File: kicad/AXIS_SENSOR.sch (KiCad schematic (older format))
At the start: 4 parts, among them U10 MPU6500

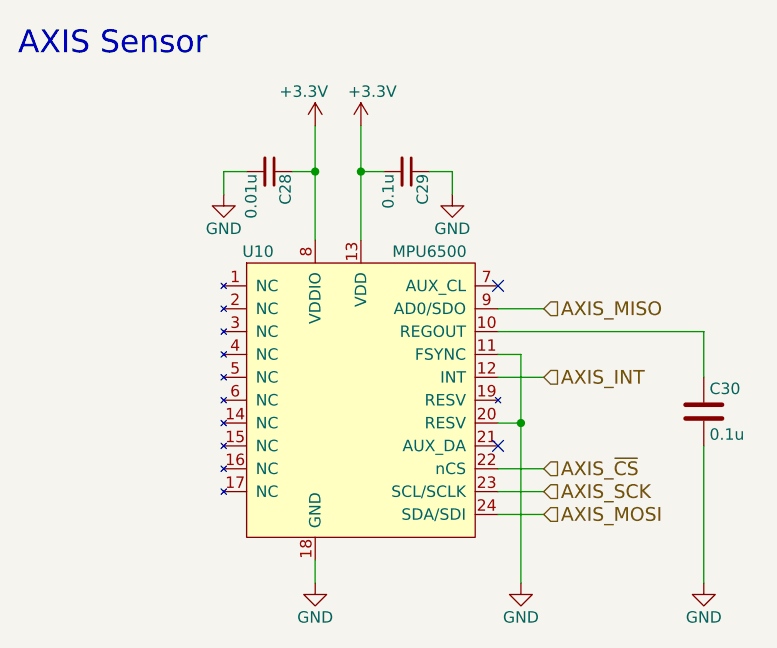
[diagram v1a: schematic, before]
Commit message: 回路図を修正
電源スイッチにPchFETを挿入
赤外線LED用FETのゲートをプルダウン
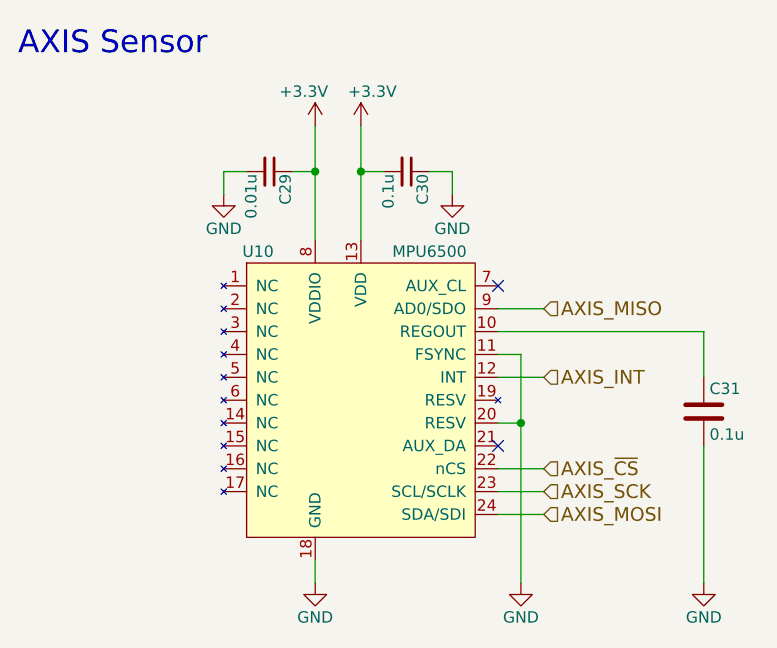
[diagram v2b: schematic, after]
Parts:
- renumbered C28 to C29, C29 to C30, C30 to C31
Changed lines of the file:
@@
 EESchema Schematic File Version 2
+LIBS:KERISEv1-rescue
 LIBS:74xgxx
 LIBS:74xx
@@
 LIBS:cmos4000
 LIBS:conn
-LIBS:connectors
 LIBS:contrib
 LIBS:cypress
@@
 LIBS:ftdi
 LIBS:gennum
-LIBS:graphic
 LIBS:hc11
-LIBS:ic-cpu
-LIBS:ic-io
-LIBS:ic-misc
-LIBS:ic-power
 LIBS:intel
 LIBS:interface
@@
 LIBS:Lattice
 LIBS:linear
-LIBS:logo
 LIBS:maxim
 LIBS:memory
@@
 LIBS:opto
 LIBS:Oscillators
-LIBS:passive
 LIBS:philips
 LIBS:power
@@
 LIBS:Zilog
 LIBS:KERISEv1
-LIBS:kerikun11
 LIBS:KERISEv1-cache
 EELAYER 25 0
@@
 $EndDescr
 $Comp
-L +3.3V #PWR78
+L +3.3V #PWR84
 U 1 1 57CCAAD0
 P 5700 2700
-F 0 "#PWR78" H 5700 2550 50  0001 C CNN
+F 0 "#PWR84" H 5700 2550 50  0001 C CNN
 F 1 "+3.3V" H 5750 2850 50  0000 C CNN
 F 2 "" H 5700 2700 50  0000 C CNN
@@
 	5700 2700 5700 3200
 $Comp
-L GND #PWR81
+L GND #PWR83
 U 1 1 57CCAAFB
 P 5500 4700
-F 0 "#PWR81" H 5500 4450 50  0001 C CNN
+F 0 "#PWR83" H 5500 4450 50  0001 C CNN
 F 1 "GND" H 5500 4550 50  0000 C CNN
 F 2 "" H 5500 4700 50  0000 C CNN
@@
 AXIS_MISO
 $Comp
-L GND #PWR82
+L GND #PWR86
 U 1 1 57CCAB79
 P 6400 4700
-F 0 "#PWR82" H 6400 4450 50  0001 C CNN
+F 0 "#PWR86" H 6400 4450 50  0001 C CNN
 F 1 "GND" H 6400 4550 50  0000 C CNN
 F 2 "" H 6400 4700 50  0000 C CNN
@@
 	6400 3700 6300 3700
 $Comp
-L C C30
+L C C31
 U 1 1 57CCABB6
 P 7200 3950
-F 0 "C30" H 7225 4050 50  0000 L CNN
+F 0 "C31" H 7225 4050 50  0000 L CNN
 F 1 "0.1u" H 7225 3850 50  0000 L CNN
 F 2 "Capacitors_SMD:C_0603" H 7238 3800 50  0001 C CNN
@@
 	7200 3600 6300 3600
 $Comp
-L GND #PWR83
+L GND #PWR87
 U 1 1 57CCAC2E
 P 7200 4700
-F 0 "#PWR83" H 7200 4450 50  0001 C CNN
+F 0 "#PWR87" H 7200 4450 50  0001 C CNN
 F 1 "GND" H 7200 4550 50  0000 C CNN
 F 2 "" H 7200 4700 50  0000 C CNN
@@
 	6500 4400 6300 4400
 $Comp
-L GND #PWR79
+L GND #PWR81
 U 1 1 57CCB3DF
 P 5100 3000
-F 0 "#PWR79" H 5100 2750 50  0001 C CNN
+F 0 "#PWR81" H 5100 2750 50  0001 C CNN
 F 1 "GND" H 5100 2850 50  0000 C CNN
 F 2 "" H 5100 3000 50  0000 C CNN
@@
 $EndComp
 $Comp
-L +3.3V #PWR77
+L +3.3V #PWR82
 U 1 1 57CCB773
 P 5500 2700
-F 0 "#PWR77" H 5500 2550 50  0001 C CNN
+F 0 "#PWR82" H 5500 2550 50  0001 C CNN
 F 1 "+3.3V" H 5450 2850 50  0000 C CNN
 F 2 "" H 5500 2700 50  0000 C CNN
@@
 	5100 2900 5200 2900
 $Comp
-L C_Small C28
+L C_Small C29
 U 1 1 57CCB95E
 P 5300 2900
-F 0 "C28" H 5310 2970 50  0000 L CNN
+F 0 "C29" H 5310 2970 50  0000 L CNN
 F 1 "0.01u" H 5310 2820 50  0000 L CNN
 F 2 "Capacitors_SMD:C_0603" H 5300 2900 50  0001 C CNN
@@
 $EndComp
 $Comp
-L C_Small C29
+L C_Small C30
 U 1 1 57CCB9B9
 P 5900 2900
-F 0 "C29" H 5910 2970 50  0000 L CNN
+F 0 "C30" H 5910 2970 50  0000 L CNN
 F 1 "0.1u" H 5910 2820 50  0000 L CNN
 F 2 "Capacitors_SMD:C_0603" H 5900 2900 50  0001 C CNN
@@
 	5800 2900 5700 2900
 $Comp
-L GND #PWR80
+L GND #PWR85
 U 1 1 57CCBA56
 P 6100 3000
-F 0 "#PWR80" H 6100 2750 50  0001 C CNN
+F 0 "#PWR85" H 6100 2750 50  0001 C CNN
 F 1 "GND" H 6100 2850 50  0000 C CNN
 F 2 "" H 6100 3000 50  0000 C CNN

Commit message: add kicad .gitignore
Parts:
- C29, C30: symbol C_Small -> KERISEv1-rescue:C_Small
- C31: symbol C -> KERISEv1-rescue:C
- U10: symbol MPU6500 -> KERISEv1:MPU6500
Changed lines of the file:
@@
-EESchema Schematic File Version 2
-LIBS:KERISEv1-rescue
-LIBS:74xgxx
-LIBS:74xx
-LIBS:ac-dc
-LIBS:actel
-LIBS:adc-dac
-LIBS:Altera
-LIBS:analog_devices
-LIBS:analog_switches
-LIBS:atmel
-LIBS:audio
-LIBS:brooktre
-LIBS:cmos_ieee
-LIBS:cmos4000
-LIBS:conn
-LIBS:contrib
-LIBS:cypress
-LIBS:dc-dc
-LIBS:device
-LIBS:digital-audio
-LIBS:diode
-LIBS:display
-LIBS:dsp
-LIBS:elec-unifil
-LIBS:ESD_Protection
-LIBS:ftdi
-LIBS:gennum
-LIBS:hc11
-LIBS:intel
-LIBS:interface
-LIBS:ir
-LIBS:Lattice
-LIBS:linear
-LIBS:maxim
-LIBS:memory
-LIBS:microchip
-LIBS:microchip_dspic33dsc
-LIBS:microchip_pic10mcu
-LIBS:microchip_pic12mcu
-LIBS:microchip_pic16mcu
-LIBS:microchip_pic18mcu
-LIBS:microchip_pic32mcu
-LIBS:microcontrollers
-LIBS:motor_drivers
-LIBS:motorola
-LIBS:msp430
-LIBS:nordicsemi
-LIBS:nxp_armmcu
-LIBS:onsemi
-LIBS:opto
-LIBS:Oscillators
-LIBS:philips
-LIBS:power
-LIBS:Power_Management
-LIBS:powerint
-LIBS:pspice
-LIBS:references
-LIBS:regul
-LIBS:relays
-LIBS:rfcom
-LIBS:sensors
-LIBS:silabs
-LIBS:siliconi
-LIBS:stm8
-LIBS:stm32
-LIBS:supertex
-LIBS:switches
-LIBS:texas
-LIBS:transf
-LIBS:transistors
-LIBS:ttl_ieee
-LIBS:valves
-LIBS:video
-LIBS:Xicor
-LIBS:xilinx
-LIBS:Zilog
-LIBS:KERISEv1
-LIBS:KERISEv1-cache
-EELAYER 25 0
+EESchema Schematic File Version 4
+EELAYER 30 0
 EELAYER END
 $Descr A4 11693 8268
@@
 $EndDescr
 $Comp
-L +3.3V #PWR84
+L power:+3.3V #PWR84
 U 1 1 57CCAAD0
 P 5700 2700
@@
 $EndComp
 Wire Wire Line
-	5700 2700 5700 3200
-$Comp
-L GND #PWR83
+	5700 2700 5700 2900
+$Comp
+L power:GND #PWR83
 U 1 1 57CCAAFB
 P 5500 4700
@@
 AXIS_MISO
 $Comp
-L GND #PWR86
+L power:GND #PWR86
 U 1 1 57CCAB79
 P 6400 4700
@@
 $EndComp
 Wire Wire Line
-	6400 4700 6400 3700
+	6400 4700 6400 4000
 Wire Wire Line
 	6400 3700 6300 3700
 $Comp
-L C C31
+L KERISEv1-rescue:C C31
 U 1 1 57CCABB6
 P 7200 3950
+AR Path="/57CCABB6" Ref="C31"  Part="1"
+AR Path="/57CC33F6/57CCABB6" Ref="C31"  Part="1"
 F 0 "C31" H 7225 4050 50  0000 L CNN
 F 1 "0.1u" H 7225 3850 50  0000 L CNN
@@
 	7200 3600 6300 3600
 $Comp
-L GND #PWR87
+L power:GND #PWR87
 U 1 1 57CCAC2E
 P 7200 4700
@@
 	6500 4400 6300 4400
 $Comp
-L GND #PWR81
+L power:GND #PWR81
 U 1 1 57CCB3DF
 P 5100 3000
@@
 $EndComp
 $Comp
-L MPU6500 U10
+L KERISEv1:MPU6500 U10
 U 1 1 57CCB62A
 P 5700 3650
@@
 $EndComp
 $Comp
-L +3.3V #PWR82
+L power:+3.3V #PWR82
 U 1 1 57CCB773
 P 5500 2700
@@
 $EndComp
 Wire Wire Line
-	5500 2700 5500 3200
+	5500 2700 5500 2900
 Wire Wire Line
 	5400 2900 5500 2900
@@
 	5100 2900 5200 2900
 $Comp
-L C_Small C29
+L KERISEv1-rescue:C_Small C29
 U 1 1 57CCB95E
 P 5300 2900
+AR Path="/57CCB95E" Ref="C29"  Part="1"
+AR Path="/57CC33F6/57CCB95E" Ref="C29"  Part="1"
 F 0 "C29" H 5310 2970 50  0000 L CNN
 F 1 "0.01u" H 5310 2820 50  0000 L CNN
@@
 $EndComp
 $Comp
-L C_Small C30
+L KERISEv1-rescue:C_Small C30
 U 1 1 57CCB9B9
 P 5900 2900
+AR Path="/57CCB9B9" Ref="C30"  Part="1"
+AR Path="/57CC33F6/57CCB9B9" Ref="C30"  Part="1"
 F 0 "C30" H 5910 2970 50  0000 L CNN
 F 1 "0.1u" H 5910 2820 50  0000 L CNN
@@
 	5800 2900 5700 2900
 $Comp
-L GND #PWR85
+L power:GND #PWR85
 U 1 1 57CCBA56
 P 6100 3000
@@
 Text Notes 4200 2400 0    100  ~ 0
 AXIS Sensor
+Wire Wire Line
+	6400 4000 6400 3700
+Wire Wire Line
+	5500 2900 5500 3200
+Wire Wire Line
+	5700 2900 5700 3200
 $EndSCHEMATC
